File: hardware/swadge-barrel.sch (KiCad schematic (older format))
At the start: 47 parts, among them J1 USB_B_Micro, Q1 Q_NPN_BEC, U1 ESP-13-WROOM-02D, U2 DISP_OLED_UG-2864HSWEG01, U3 BUS_PCIexpress, U4 QMA6981, U5 AP1117-33

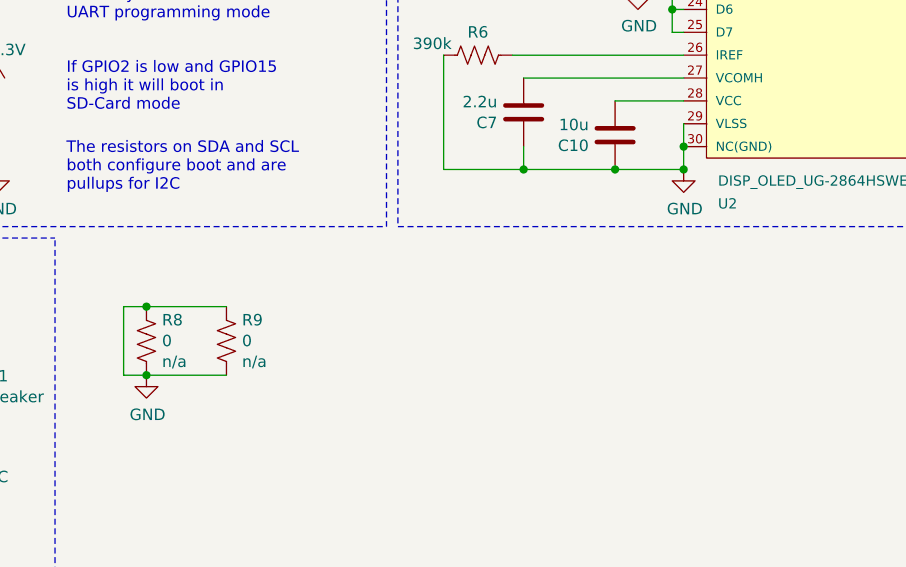
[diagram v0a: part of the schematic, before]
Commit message: Added BOM descriptions:
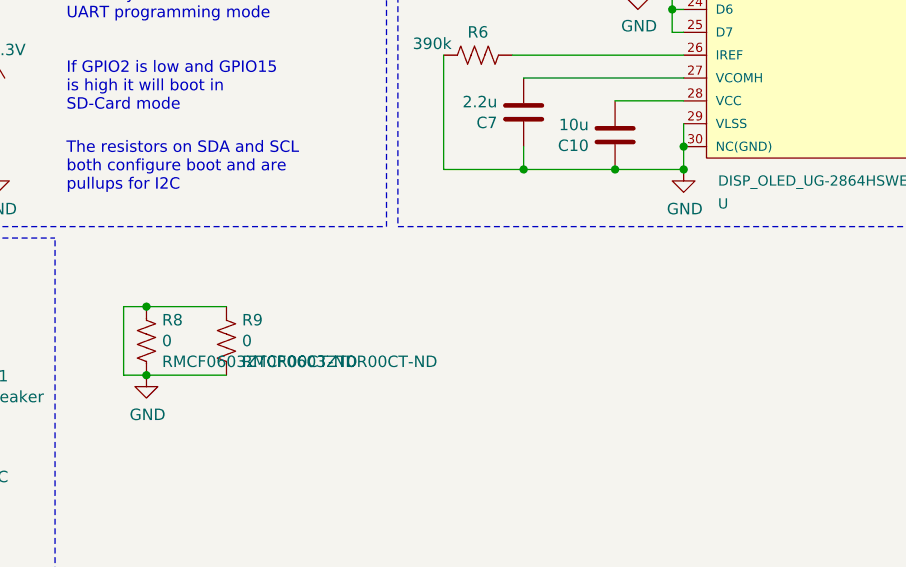
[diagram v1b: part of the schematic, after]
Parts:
- BT1, BT2: Notes (none) -> Use through-hole AA Battery Holder in Style of Keystone 2460
- C18: Digikey 1276-1000-1-ND -> 1276-1085-1-ND
- D1, D2, D3, D4, D5, D6: Notes Digikey item is x10 -> Use WS2812B LED, Digikey item is x10
- J1: Notes (none) -> Must use micro USB SMT-only Header
- LS1: Digikey https://lcsc.com/product-detail/Buzzers_Jiangsu-Huaneng-Ele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 -> LCSC Part #C96102
- R8, R9: Digikey n/a -> RMCF0603ZT0R00CT-ND
- S1: Notes (none) -> Use standard SMT box tactile buttons. Similar to PTS645SM43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
- S2, S3: Notes (none) -> Use standard 12mmx12mm SMT box tactile buttons with flat to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
- S4: Notes (none) -> Use SPDT slide switch
- U: renamed from U2; Digikey 541-3486-ND -> 541-3485-ND; Notes (none) -> This is two parts: display and connector. Display must be o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
- U1: Notes (none) -> Use ESP-WROOM-02D
- U4: Notes (none) -> Use https://lcsc.com/product-detail/Others_QST-QMA6981_C310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
- U5: Notes (none) -> Use any 1117 3.3V SOT-223 regulator. I.e. AZ1117 or AP1117
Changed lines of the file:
@@
 F 4 "45" H 0   0   50  0001 C CNN "Cost100"
 F 5 "1528-1104-ND" H 0   0   50  0001 C CNN "Digikey"
-F 6 "Digikey item is x10" H 0   0   50  0001 C CNN "Notes"
+F 6 "Use WS2812B LED, Digikey item is x10" H 0   0   50  0001 C CNN "Notes"
 F 7 "Y" H 0   0   50  0001 C CNN "Substitutable"
 	1    4300 1650
@@
 F 4 "45" H 0   0   50  0001 C CNN "Cost100"
 F 5 "1528-1104-ND" H 0   0   50  0001 C CNN "Digikey"
-F 6 "Digikey item is x10" H 0   0   50  0001 C CNN "Notes"
+F 6 "Use WS2812B LED, Digikey item is x10" H 0   0   50  0001 C CNN "Notes"
 F 7 "Y" H 0   0   50  0001 C CNN "Substitutable"
 	1    4950 1650
@@
 F 4 "45" H 0   0   50  0001 C CNN "Cost100"
 F 5 "1528-1104-ND" H 0   0   50  0001 C CNN "Digikey"
-F 6 "Digikey item is x10" H 0   0   50  0001 C CNN "Notes"
+F 6 "Use WS2812B LED, Digikey item is x10" H 0   0   50  0001 C CNN "Notes"
 F 7 "Y" H 0   0   50  0001 C CNN "Substitutable"
 	1    5600 1650
@@
 F 4 "45" H 0   0   50  0001 C CNN "Cost100"
 F 5 "1528-1104-ND" H 0   0   50  0001 C CNN "Digikey"
-F 6 "Digikey item is x10" H 0   0   50  0001 C CNN "Notes"
+F 6 "Use WS2812B LED, Digikey item is x10" H 0   0   50  0001 C CNN "Notes"
 F 7 "Y" H 0   0   50  0001 C CNN "Substitutable"
 	1    6250 1650
@@
 F 4 "45" H 0   0   50  0001 C CNN "Cost100"
 F 5 "1528-1104-ND" H 0   0   50  0001 C CNN "Digikey"
-F 6 "Digikey item is x10" H 0   0   50  0001 C CNN "Notes"
+F 6 "Use WS2812B LED, Digikey item is x10" H 0   0   50  0001 C CNN "Notes"
 F 7 "Y" H 0   0   50  0001 C CNN "Substitutable"
 	1    6900 1650
@@
 F 4 "45" H 0   0   50  0001 C CNN "Cost100"
 F 5 "1528-1104-ND" H 0   0   50  0001 C CNN "Digikey"
-F 6 "Digikey item is x10" H 0   0   50  0001 C CNN "Notes"
+F 6 "Use WS2812B LED, Digikey item is x10" H 0   0   50  0001 C CNN "Notes"
 F 7 "Y" H 0   0   50  0001 C CNN "Substitutable"
 	1    7550 1650
@@
 F 5 "AP2114H-3.3TRG1DICT-ND" H 0   0   50  0001 C CNN "Digikey"
 F 6 "Y" H 0   0   50  0001 C CNN "Substitutable"
+F 7 "Use any 1117 3.3V SOT-223 regulator.  I.e. AZ1117 or AP1117" H 10350 1150 50  0001 C CNN "Notes"
 	1    10350 1150
 	1    0    0    -1
@@
 F 5 "WM17141CT-ND" H 0   0   50  0001 C CNN "Digikey"
 F 6 "Y" H 0   0   50  0001 C CNN "Substitutable"
+F 7 "Must use micro USB SMT-only Header" H 9650 1150 50  0001 C CNN "Notes"
 	1    9650 1150
 	1    0    0    -1
@@
 Wire Wire Line
 	10650 1150 10650 1400
-$Comp
-L Swadge_Parts:DISP_OLED_UG-2864HSWEG01 U2
-U 1 1 5C3C7BBF
-P 5950 4050
-F 0 "U2" H 5100 2300 45  0000 L CNN
-F 1 "DISP_OLED_UG-2864HSWEG01" H 5100 2400 45  0000 L CNN
-F 2 "Swadge_Parts:oled-flat_copy" H 5980 4200 20  0001 C CNN
-F 3 "http://www.vishay.com/docs/37903/oled128o064dgpp3n00000.pdf" H 5950 4050 50  0001 C CNN
-F 4 "988" H 0   0   50  0001 C CNN "Cost100"
-F 5 "541-3486-ND" H 0   0   50  0001 C CNN "Digikey"
-F 6 "Y" H 0   0   50  0001 C CNN "Substitutable"
-F 7 "https://cdn-shop.adafruit.com/datasheets/UG-2864HSWEG01.pdf" H 0   0   50  0001 C CNN "Adafruit"
-	1    5950 4050
-	1    0    0    -1
-$EndComp
 $Comp
 L Swadge_Parts:C C10
@@
 $EndComp
 Wire Wire Line
-	4950 3050 4050 3050
-Wire Wire Line
 	4950 2950 4350 2950
 Wire Wire Line
@@
 F 5 "450-1759-1-ND" H -5400 -2150 50  0001 C CNN "Digikey"
 F 6 "Y" H -5400 -2150 50  0001 C CNN "Substitutable"
-F 7 "Switch Tactile OFF _ON_ SPST Round Button Gull Wing 0.05A 24VDC 1VA 9.18N SMD T/R" H -5400 -2150 50  0001 C CNN "Description"
-F 8 "FSM4JSMATR" H -5400 -2150 50  0001 C CNN "MPN"
-F 9 "TE Connectivity" H -5400 -2150 50  0001 C CNN "Manufacturer"
+F 7 "Switch Tactile OFF _ON_ SPST Round Button Gull Wing 0.05A 24VDC 1VA 9.18N SMD T/R" H 2150 1950 50  0001 C CNN "Description"
+F 8 "FSM4JSMATR" H 2150 1950 50  0001 C CNN "MPN"
+F 9 "TE Connectivity" H 2150 1950 50  0001 C CNN "Manufacturer"
+F 10 "Use standard SMT box tactile buttons.  Similar to PTS645SM43SMTR92." H 2150 1950 50  0001 C CNN "Notes"
 	1    2150 1950
 	1    0    0    -1
@@
 	1900 1850 1900 2050
 Wire Wire Line
-	4950 5450 4950 5550
-Wire Wire Line
 	2400 1850 2400 2050
-Connection ~ 4950 5550
-Wire Wire Line
-	4950 5550 4950 5650
 Connection ~ 2400 2050
 Wire Wire Line
@@
 F 5 "36-2460-ND" H 0   0   50  0001 C CNN "Digikey"
 F 6 "Y" H 0   0   50  0001 C CNN "Substitutable"
+F 7 "Use through-hole AA Battery Holder in Style of Keystone 2460" H 10450 2000 50  0001 C CNN "Notes"
 	1    10450 2000
 	0    1    1    0
@@
 F 5 "36-2460-ND" H 0   0   50  0001 C CNN "Digikey"
 F 6 "Y" H 0   0   50  0001 C CNN "Substitutable"
+F 7 "Use through-hole AA Battery Holder in Style of Keystone 2460" H 10000 2000 50  0001 C CNN "Notes"
 	1    10000 2000
 	0    1    1    0
@@
 F 5 "270" H 2000 3650 50  0001 C CNN "Cost100"
 F 6 "Y" H 2000 3650 50  0001 C CNN "Substitutable"
+F 7 "Use ESP-WROOM-02D" H 2000 3650 50  0001 C CNN "Notes"
 	1    2000 3650
 	1    0    0    -1
@@
 F 5 "36" H 7450 6550 50  0001 C CNN "Cost100"
 F 6 "Y" H 7450 6650 50  0001 C CNN "Substitutable"
+F 7 "Use https://lcsc.com/product-detail/Others_QST-QMA6981_C310611.html " H 7900 5650 50  0001 C CNN "Notes"
 	1    7900 5650
 	1    0    0    -1
@@
 F 3 "" H 9200 5950 50  0001 C CNN
 F 4 "10" H 6350 -1000 50  0001 C CNN "Cost100"
-F 5 "1276-1000-1-ND" H 6350 -1000 50  0001 C CNN "Digikey"
+F 5 "1276-1085-1-ND" H 6350 -1000 50  0001 C CNN "Digikey"
 F 6 "Y" H 6350 -1000 50  0001 C CNN "Substitutable"
 	1    9200 5950
@@
 F 5 "76" H 2600 1600 50  0001 C CNN "Cost100"
 F 6 "Y" H 2450 1650 50  0001 C CNN "Substitutable"
+F 7 "Use standard 12mmx12mm SMT box tactile buttons with flat top. Similar to TL3300DF160Q." H 2300 1150 50  0001 C CNN "Notes"
 	1    2300 1150
 	1    0    0    -1
@@
 F 5 "76" H 1250 1600 50  0001 C CNN "Cost100"
 F 6 "Y" H 1100 1650 50  0001 C CNN "Substitutable"
+F 7 "Use standard 12mmx12mm SMT box tactile buttons with flat top. Similar to TL3300DF160Q." H 950 1150 50  0001 C CNN "Notes"
 	1    950  1150
 	1    0    0    -1
@@
 F 5 "401-2016-1-ND" H 0   0   50  0001 C CNN "Digikey"
 F 6 "Y" H 0   0   50  0001 C CNN "Substitutable"
+F 7 "Use SPDT slide switch" H 10850 1500 50  0001 C CNN "Notes"
 	1    10850 1500
 	-1   0    0    1
@@
 F 2 "Swadge_Parts:Speaker_9mm" H 1700 6350 50  0001 C CNN
 F 3 "https://datasheet.lcsc.com/szlcsc/Jiangsu-Huaneng-Elec-HNB09A03_C96102.pdf" H 1690 6500 50  0001 C CNN
-F 4 "https://lcsc.com/product-detail/Buzzers_Jiangsu-Huaneng-Elec-HNB09A03_C96102.html" H 1300 6900 50  0001 C CNN "Digikey"
+F 4 "LCSC Part #C96102" H 1300 6900 50  0001 C CNN "Digikey"
 F 5 "13.48" H 1950 6800 50  0001 C CNN "Cost100"
 F 6 "Y" H 1950 7050 50  0001 C CNN "Substitutable"
@@
 F 2 "Swadge_Parts:R_0603_1608Metric" V 2640 6390 50  0001 C CNN
 F 3 "~" V 2700 6400 50  0001 C CNN
-F 4 "n/a" H 2668 6309 50  0000 L CNN "Digikey"
+F 4 "RMCF0603ZT0R00CT-ND" H 2668 6309 50  0000 L CNN "Digikey"
 F 5 "10" H 2600 6400 10  0001 C CNN "Cost100"
 F 6 "Y" H 2600 6400 10  0001 C CNN "Substitutable"
@@
 F 2 "Swadge_Parts:R_0603_1608Metric" V 2990 6390 50  0001 C CNN
 F 3 "~" V 3050 6400 50  0001 C CNN
-F 4 "n/a" H 3018 6309 50  0000 L CNN "Digikey"
+F 4 "RMCF0603ZT0R00CT-ND" H 3018 6309 50  0000 L CNN "Digikey"
 F 5 "10" H 2950 6400 10  0001 C CNN "Cost100"
 F 6 "Y" H 2950 6400 10  0001 C CNN "Substitutable"
@@
 Wire Wire Line
 	7950 3950 7900 3950
+Connection ~ 4950 5550
+Wire Wire Line
+	4950 5550 4950 5650
+Wire Wire Line
+	4950 5450 4950 5550
+Wire Wire Line
+	4950 3050 4050 3050
+$Comp
+L Swadge_Parts:DISP_OLED_UG-2864HSWEG01 U
+U 1 1 5C3C7BBF
+P 5950 4050
+F 0 "U" H 5100 2300 45  0000 L CNN
+F 1 "DISP_OLED_UG-2864HSWEG01" H 5100 2400 45  0000 L CNN
+F 2 "Swadge_Parts:oled-flat_copy" H 5980 4200 20  0001 C CNN
+F 3 "https://lcsc.com/product-detail/_WiseChip-VG-2864KSWEG01_C194313.html" H 5950 4050 50  0001 C CNN
+F 4 "988" H 0   0   50  0001 C CNN "Cost100"
+F 5 "541-3485-ND" H 0   0   50  0001 C CNN "Digikey"
+F 6 "Y" H 0   0   50  0001 C CNN "Substitutable"
+F 7 "https://cdn-shop.adafruit.com/datasheets/UG-2864HSWEG01.pdf" H 0   0   50  0001 C CNN "Adafruit"
+F 8 "This is two parts: display and connector. Display must be one color, white, with SSD1306 driver, 0.96\". Both display and connector must have top contacts. https://www.buydisplay.com/default/128x64-oled-i2c-0-96-display-white-color-connector-fpc-ssd1306 https://lcsc.com/product-detail/FFC-FPC-Connectors_JUSHUO-AFC07-S30ECC-00_C11095.html" H 5950 4050 50  0001 C CNN "Notes"
+	1    5950 4050
+	1    0    0    -1
+$EndComp
 $EndSCHEMATC

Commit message: Finished BOM notes
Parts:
- added U2: OLED_DISPLAY, Swadge_Parts:NULL, symbol Swadge_Parts:OLED_DISPLAY
- C1, C10, C11, C12, C13, C14, C15, C16, C17, C18, C2, C3, C7, C8, R1, R2, R3, R4, R5, R6, R7: Notes (none) -> 0603 Package
- C4, C5, C6, C9: Digikey 1276-1036-1-ND -> 1276-1097-1-ND; Notes (none) -> 1206 Package, must be at least 1.5mm tall, may be taller. 1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
- LS1: footprint Swadge_Parts:Speaker_9mm -> Swadge_Parts:Buzzer_12x9.5RM7.6; Digikey LCSC Part #C96102 -> https://lcsc.com/product-detail/Buzzers_Jiangsu-Huaneng-Ele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; Notes (none) -> Use magnetic buzzer, 3V rated, 9mm diameter, 5mm between th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
- Q1: Notes (none) -> Use any NPN transistor in SOT-23 package with the same lead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
- R8, R9: Notes (none) -> 0603 Package, must not be taller than 0.8mm, this sits unde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
- S1: MPN FSM4JSMATR -> (none); Manufacturer TE Connectivity -> (none)
- SW1: renamed from S4; Notes Use SPDT slide switch -> Use SPDT slide switch. Similar to PCM12SMTR
- U6: renamed from U; value DISP_OLED_UG-2864HSWEG01 -> OLED_CONNECTOR; symbol Swadge_Parts:DISP_OLED_UG-2864HSWEG01 -> Swadge_Parts:OLED_CONNECTOR; Adafruit https://cdn-shop.adafruit.com/datasheets/UG-2864HSWEG01.pdf -> (none); Cost100 988 -> 119; Digikey 541-3485-ND -> LCSC #C11095; Notes This is two parts: display and connector. Display must be o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 -> Must have top contacts, same as the OLED
